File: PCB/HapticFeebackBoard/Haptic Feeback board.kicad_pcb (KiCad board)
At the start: 2 copper layers, 46 x 41 mm, 12 parts, among them J1 1769, J2 Conn_01x02, M1 Conn_01x02, M2 Conn_01x02, Q1 2N7002E, SW1 PTS526 SM15 SMTR2 LFS

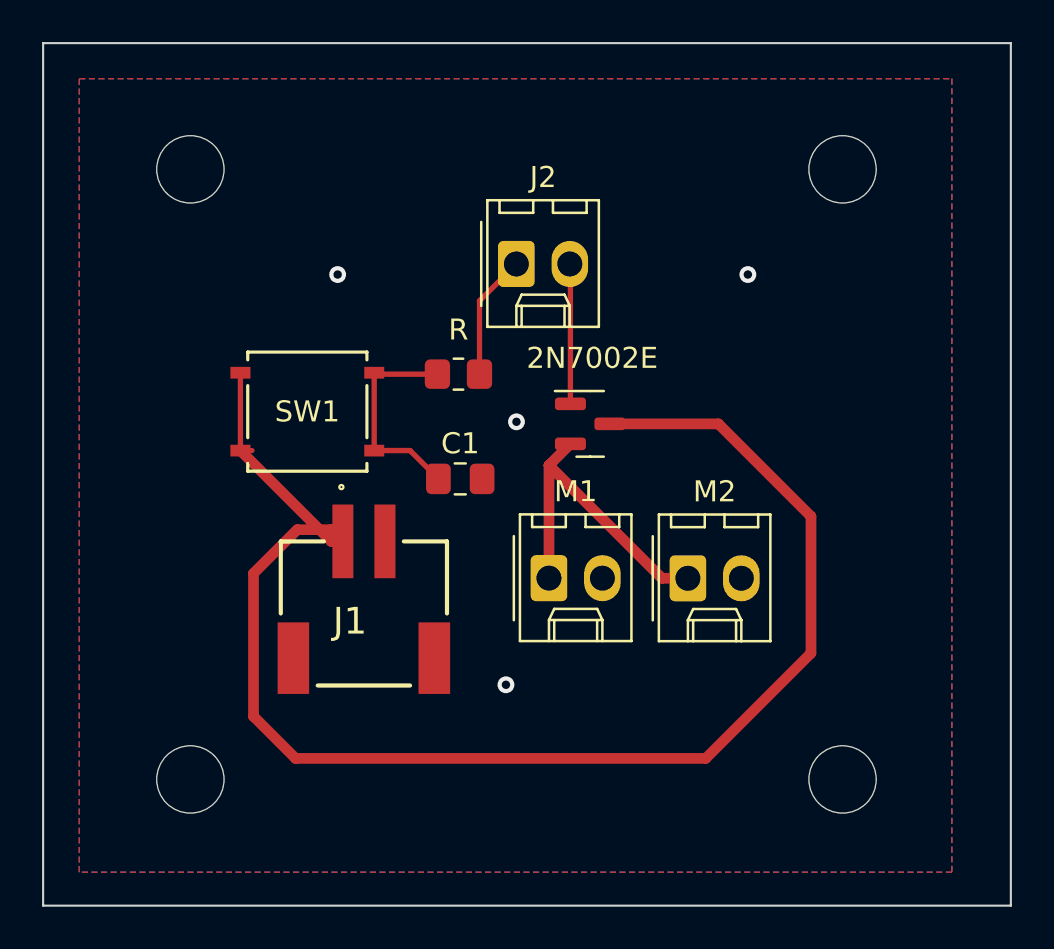
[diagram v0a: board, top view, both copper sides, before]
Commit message: Further minor edits, added power LED
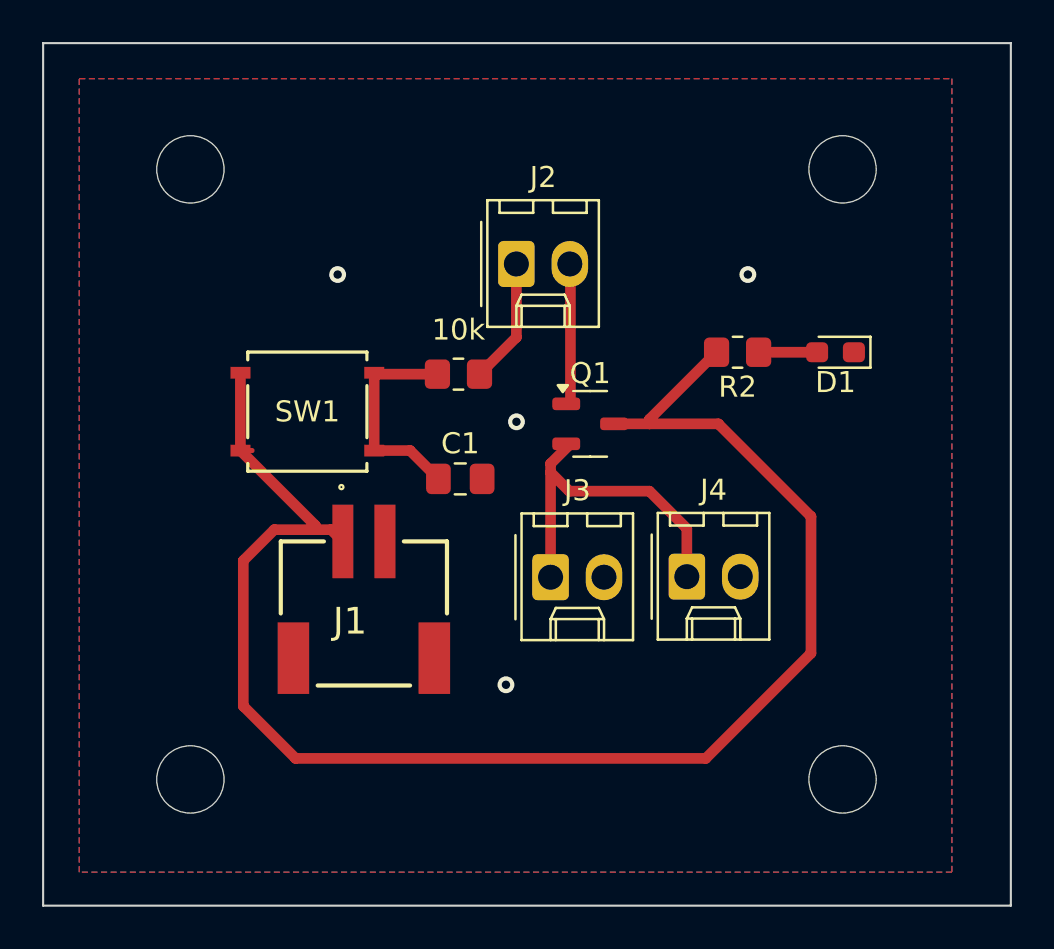
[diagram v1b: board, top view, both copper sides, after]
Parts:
- removed M1, M2: Conn_01x02, Connector_Molex:Molex_KK-254_AE-6410-02A_1x02_P2.54mm_Vertical
- added D1: LED(Red), LED_SMD:LED_0603_1608Metric_Pad1.05x0.95mm_HandSolder, F.Cu at (156.2, 91.7)
- added J3: Conn_01x02, Connector_Molex:Molex_KK-254_AE-6410-02A_1x02_P2.54mm_Vertical, F.Cu at (142.6, 102.4)
- added J4: Conn_01x02, Connector_Molex:Molex_KK-254_AE-6410-02A_1x02_P2.54mm_Vertical, F.Cu at (149.1, 102.4)
- added R2: 10k, Resistor_SMD:R_0805_2012Metric_Pad1.20x1.40mm_HandSolder, F.Cu at (151.5, 91.7)
- Q1: footprint Package_TO_SOT_SMD:SOT-23 -> Package_TO_SOT_SMD:SOT-23-3
- R1: value R -> 10k
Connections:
- net /BMS Power renamed +3.3V
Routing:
- net +3.3V: track 70.3 -> 74.7 mm
- net Net-(D1-A): track 0.00 -> 2.78 mm
- net /Motor1: track 15.6 -> 16.6 mm
